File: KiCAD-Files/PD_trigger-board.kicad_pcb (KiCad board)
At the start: 2 copper layers, 18 x 23.5 mm, 16 parts, among them J1 USB_C_Receptacle_USB3.0_12P, U1 HUSB238, U2 SI4459ADY-T1-GE3, U3 ESP32-S3-mini_pinprofile

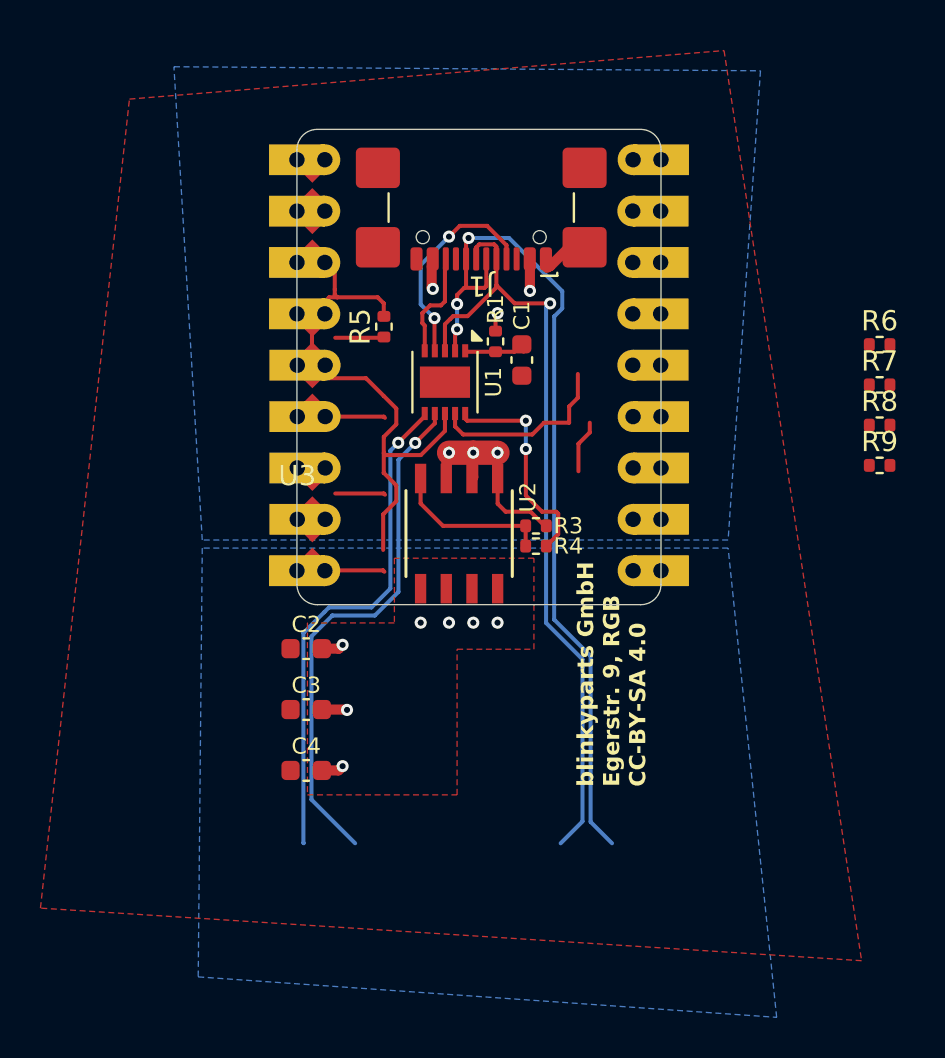
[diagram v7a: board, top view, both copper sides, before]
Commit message: Layout completed, ToDo processed
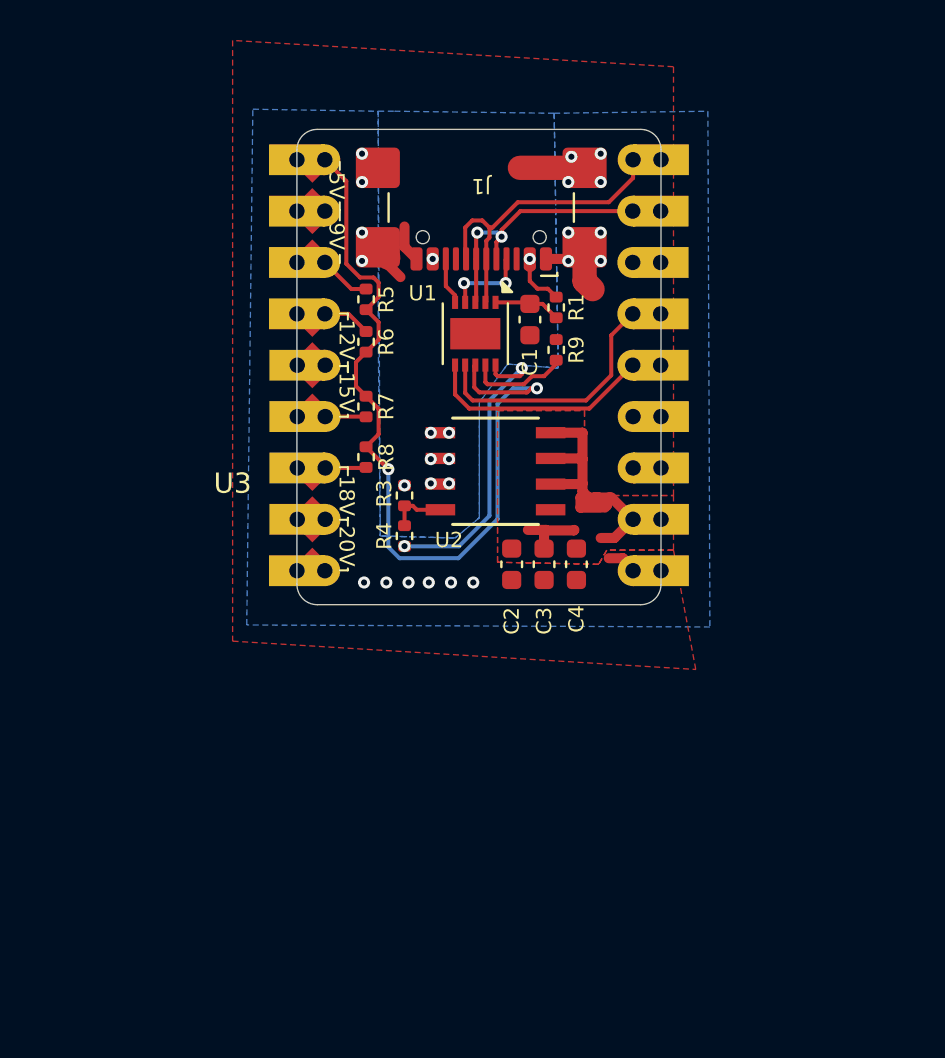
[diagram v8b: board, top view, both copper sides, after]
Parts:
- moved R8 25.4 mm to (134.5, 92.3), turned to -90 degrees
- moved R7 25.4 mm to (134.5, 89.8), turned to -90 degrees
- moved R6 25.4 mm to (134.5, 86.6), turned to 90 degrees
- moved R9 17.0 mm to (143.9, 87.0), turned to 90 degrees
- moved C4 16.8 mm to (144.9, 97.6), turned to -90 degrees
- moved C3 13.8 mm to (143.3, 97.6), turned to -90 degrees
- moved C2 11.0 mm to (141.7, 97.6), turned to -90 degrees
- moved R3 6.67 mm to (136.4, 94.2), turned to -90 degrees
- moved R4 6.52 mm to (136.4, 96.2), turned to -90 degrees
- moved U2 3.57 mm to (140.9, 93.0), turned to 0 degrees
- moved R1 3.44 mm to (143.9, 84.9)
- moved U1 2.83 mm to (139.9, 86.2)
- moved C1 2.04 mm to (142.6, 85.5)
- moved R5 1.61 mm to (134.5, 84.5)
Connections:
- U3 pad 12: SCL -> unconnected-(U3-Pad12)
- U3 pad 13: SDA -> unconnected-(U3-Pad13)
- U3 pad 14: GND -> SDA
- U3 pad 15: D- -> SCL
- U3 pad 16: D+ -> GND
- U3 pad 17: unconnected-(U3-UNSET-Pad17) -> D-
- U3 pad 18: unconnected-(U3-UNSET-Pad18) -> D+
- U3 pad 9: GND -> unconnected-(U3-SET_20V-Pad9)
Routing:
- net GND: track 3.98 -> 30.9 mm, vias 0 -> 18
- net D-: track 39.7 -> 13.3 mm, vias 1 -> 2
- net D+: track 42.2 -> 15.9 mm, vias 3 -> 0
- net VOUT: track 3.50 -> 19.0 mm, vias 7 -> 0
- net SDA: track 25.0 -> 11.4 mm, vias 1 -> 0
- net VSET: track 28.7 -> 41.6 mm, vias 0 -> 2
- net SCL: track 25.9 -> 13.2 mm, vias 1 -> 0
- net VBUS: track 13.7 -> 6.80 mm, vias 6 -> 9
- net CC1: track 11.0 -> 4.29 mm
- net (no net): track 5.12 -> 0.00 mm
- net Net-(U2-G): track 7.92 -> 2.84 mm
- net Net-(U1-ISET): track 9.27 -> 5.00 mm
- net GATE: track 10.8 -> 14.9 mm
- net Net-(U3-SET_9V): track 0.00 -> 2.58 mm
- net CC2: track 5.02 -> 2.49 mm
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- added copper zone on B.Cu, net GND
- removed copper zone on B.Cu, net VOUT
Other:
- board text added: "12V"
- board text added: "15V"
- board text added: "18V"
- board text added: "20V"
- board text added: "5V"
- board text added: "9V"
- board text added: "PD-Trigger-Board v0.2 PD V2.0"
- board text removed: "J7: 5V J8: 9V J9: 12V J10: 15V J11: 18V"
